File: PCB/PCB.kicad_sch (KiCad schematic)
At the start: 60 parts, among them J1 USB_C_Receptacle_USB2.0_16P, Q2 IRLML2060, SW1 SW_Push, SW2 SW_Push, U1 RP2040, U2 USBLC6-2SC6, U3 NCP1117ST33T3G, U4 W25Q32JVSS, U5 Conn, U6 ST25DV04K-JFR6D3, Y1 Crystal_GND24

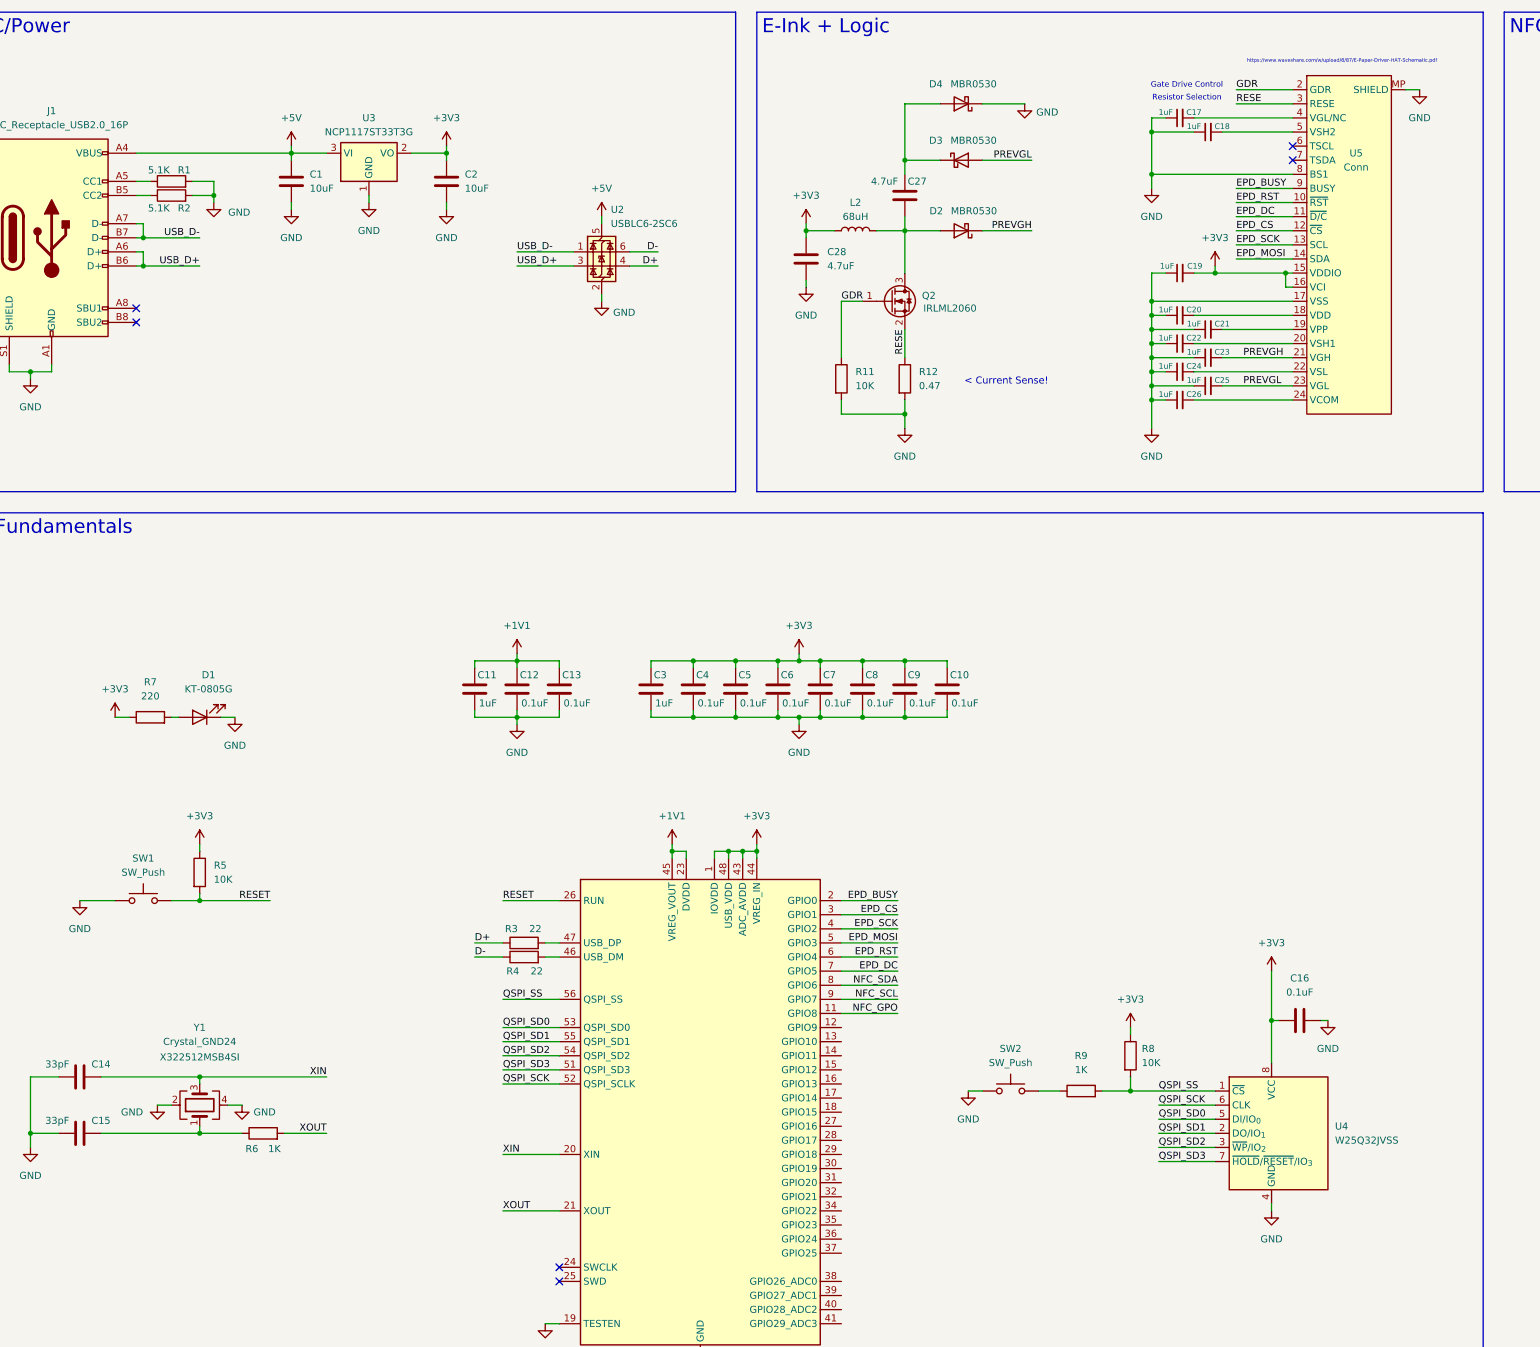
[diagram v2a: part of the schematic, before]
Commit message: added in the buttons, stole them from @cheyao :D
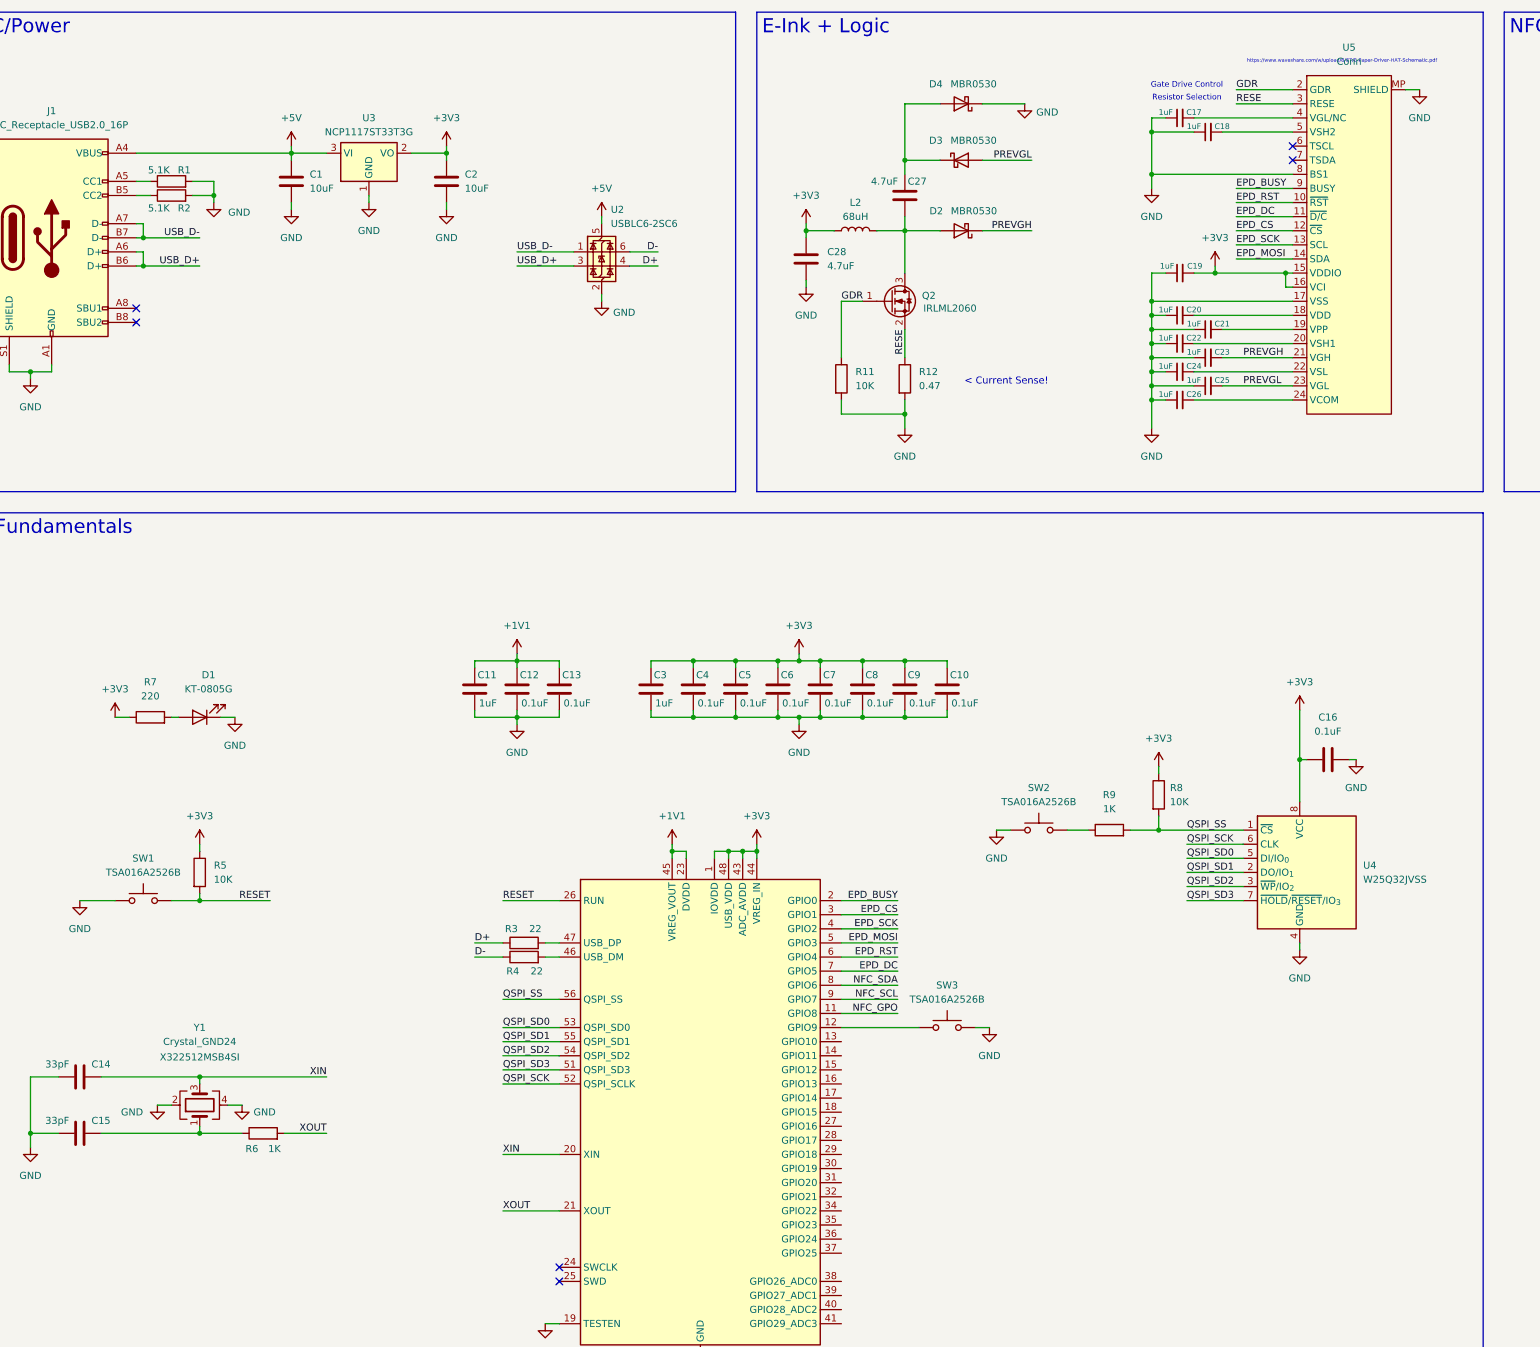
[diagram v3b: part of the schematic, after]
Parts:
- removed U5: Conn, inkbadge:LCSC_1x24-1MP_P0.5mm_Horizontal, symbol inkbadge:EINK-2.9inch
- added SW3: TSA016A2526B, kai's library:SW_Push_SPST_TSA016, symbol Switch:SW_Push
- added U5: Conn, kai's library:LCSC_1x24-1MP_P0.5mm_Horizontal, symbol kai-library:EINK-2.9inch
- J1: footprint (none) -> Connector_USB:USB_C_Receptacle_HRO_TYPE-C-31-M-12
- SW1, SW2: value SW_Push -> TSA016A2526B; footprint (none) -> kai's library:SW_Push_SPST_TSA016
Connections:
- net +3V3: now also U5.15 (VDDIO), U5.16 (VCI)
- net EPD_BUSY: now also U5.9 (BUSY)
- net EPD_CS: now also U5.12 (~{CS})
- net EPD_DC: now also U5.11 (~{D/C})
- net EPD_MOSI: now also U5.14 (SDA)
- net EPD_RST: now also U5.10 (~{RST})
- net EPD_SCK: now also U5.13 (SCL)
- net GDR: now also U5.2 (GDR)
- net GND: now also SW3.2, U5.17 (VSS), U5.8 (BS1), U5.MP (SHIELD)
- net PREVGH: now also U5.21 (VGH)
- net PREVGL: now also U5.23 (VGL)
- net RESE: now also U5.3 (RESE)
- net at U1.12 (GPIO9): now also SW3.1
- net at C20.2: now also U5.18 (VDD)
- net at C17.2: now also U5.4 (VGL/NC)
- net at C21.2: now also U5.19 (VPP)
- net at C22.2: now also U5.20 (VSH1)
- net at C24.2: now also U5.22 (VSL)
- net at C26.2: now also U5.24 (VCOM)
- net at C18.2: now also U5.5 (VSH2)
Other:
- moved on the sheet: C16, R8, R9, SW2, U4

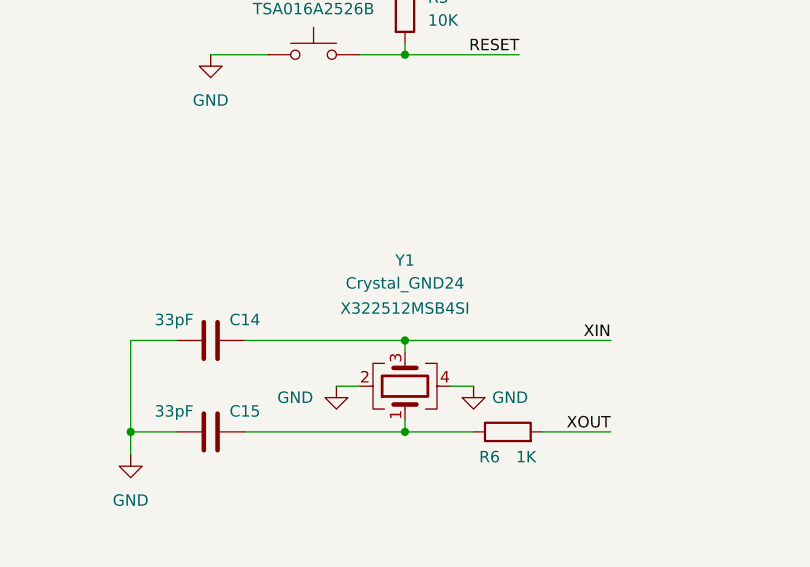
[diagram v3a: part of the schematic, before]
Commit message: finished all the footprints, found an inductor
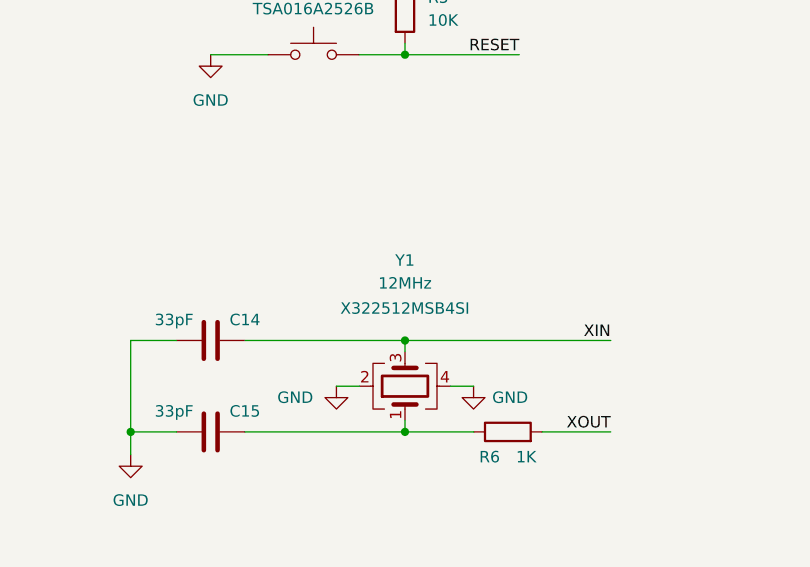
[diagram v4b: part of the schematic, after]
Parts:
- L2: footprint (none) -> Inductor_SMD:L_Sunlord_SWPA252010S; MPN (none) -> SWPA6045S680MT
- Y1: value Crystal_GND24 -> 12MHz; footprint (none) -> Crystal:Crystal_SMD_3225-4Pin_3.2x2.5mm
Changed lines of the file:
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@@
 			)
 		)
-		(property "Value" "Crystal_GND24"
+		(property "Value" "12MHz"
 			(at 62.23 200.66 90)
 			(effects
@@
 			)
 		)
-		(property "Footprint" ""
+		(property "Footprint" "Crystal:Crystal_SMD_3225-4Pin_3.2x2.5mm"
 			(at 62.23 212.09 0)
 			(effects
@@
 			)
 		)
-		(property "Footprint" ""
+		(property "Footprint" "Inductor_SMD:L_Sunlord_SWPA252010S"
 			(at 180.34 54.61 0)
 			(effects
@@
 			(effects
 				(font
+					(size 1.27 1.27)
+				)
+				(hide yes)
+			)
+		)
+		(property "MPN" "SWPA6045S680MT"
+			(at 180.34 54.61 90)
+			(effects
+				(font
